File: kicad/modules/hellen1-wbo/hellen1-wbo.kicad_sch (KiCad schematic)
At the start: 59 parts, among them J600 Conn_02x03_Odd_Even, M600 Module-wbo-0.3, Q600 BTS3028, Q601 VNP28N04-E, U600 MCP6004, U601 AD8628, U602 STM32F042K6Tx, U603 REF3033, U604 XC6206P332MR

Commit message: add can
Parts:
- added C617, C618: 100n, Capacitor_SMD:C_0402_1005Metric, symbol hellen1-wbo-rescue:C-Device
- added D603: PESD1CAN, Package_TO_SOT_SMD:SOT-23, symbol semiconductors:PESD1CAN
- added R629: 120, Resistor_SMD:R_0402_1005Metric, symbol hellen1-wbo-rescue:R-Device
- added U605: TJA1051T/3/1J, Package_SO:SO-8_3.9x4.9mm_P1.27mm, symbol Transceivers:TJA1051T/3/1J
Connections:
- net +5V: now also C617.1, U605.3 (VCC)
- net CAN_RX: now also U605.4 (RXD)
- net CAN_TX: now also U605.1 (TXD)
- net GND: now also C617.2, C618.2, D603.3 (S), U605.2 (GND), U605.8 (S)
- new net CANH: D603.2 (D), R629.1, U605.6 (CANL)
- new net CANL: D603.1 (G), R629.2, U605.7 (CANH)
- new net CANVIO: C618.1, U605.5 (VIO)
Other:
- moved on the sheet: C605, R607, R610, R611, R612, U600C

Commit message: adding CAN
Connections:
- net CANVIO is gone; now on net +3V3: C618.1, U605.5 (VIO)
- net CANH: now also M600.W3 (CANH)
- net CANL: now also M600.W4 (CANL)
- net CAN_RX: no longer M600.W3 (CAN_RX)
- net CAN_TX: no longer M600.W4 (CAN_TX)
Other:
- moved on the sheet: C617, C618, D603, R629, U605

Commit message: new wbo module
правки

финал
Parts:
- M600: value Module-wbo-0.3 -> Module-wbo-0.4; footprint hellen-one-wbo-0.3:wbo -> hellen-one-wbo-0.4:wbo; symbol hellen-one-wbo-0.3:Module-wbo-0.3 -> hellen-one-wbo-0.4:Module-wbo-0.4
- renumbered D603 to D604
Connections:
- net GND: now also U602.2 (PF0), U602.3 (PF1)
- no-connect marks 11 -> 9
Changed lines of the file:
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@@
   (junction (at 68.58 114.3) (diameter 0) (color 0 0 0 0)
   )
+  (junction (at 175.895 85.09) (diameter 0) (color 0 0 0 0)
+  )
   (junction (at 186.055 61.595) (diameter 1.016) (color 0 0 0 0)
   )
@@
   (no_connect (at 175.895 97.79))
   (no_connect (at 201.295 107.95))
-  (no_connect (at 175.895 82.55))
   (no_connect (at 201.295 92.71))
   (no_connect (at 201.295 95.25))
@@
   (no_connect (at 261.62 35.56))
   (no_connect (at 201.295 82.55))
-  (no_connect (at 175.895 85.09))
   (no_connect (at 201.295 80.01))
   (wire (pts (xy 64.77 123.19) (xy 64.77 111.76))
@@
     (stroke (width 0) (type solid) (color 0 0 0 0))
   )
+  (wire (pts (xy 171.45 85.09) (xy 175.895 85.09))
+    (stroke (width 0) (type solid) (color 0 0 0 0))
+  )
   (wire (pts (xy 120.65 87.63) (xy 118.11 87.63))
     (stroke (width 0) (type solid) (color 0 0 0 0))
@@
     (stroke (width 0) (type solid) (color 0 0 0 0))
   )
+  (wire (pts (xy 175.895 85.09) (xy 175.895 82.55))
+    (stroke (width 0) (type default) (color 0 0 0 0))
+  )
   (wire (pts (xy 27.94 32.385) (xy 27.94 34.925))
     (stroke (width 0) (type solid) (color 0 0 0 0))
@@
     (pin "1")
   )
+  (symbol (lib_id "hellen1-wbo-rescue:GND-power") (at 171.45 85.09 0) (mirror y) (unit 1)
+    (in_bom yes) (on_board yes)
+    (property "Reference" "#PWR?" (id 0) (at 171.45 91.44 0)
+      (effects (font (size 1.27 1.27)) hide)
+    )
+    (property "Value" "GND" (id 1) (at 171.323 89.4842 0))
+    (property "Footprint" "" (id 2) (at 171.45 85.09 0)
+      (effects (font (size 1.27 1.27)) hide)
+    )
+    (property "Datasheet" "" (id 3) (at 171.45 85.09 0)
+      (effects (font (size 1.27 1.27)) hide)
+    )
+    (pin "1")
+  )
   (symbol (lib_id "hellen1-wbo-rescue:GND-power") (at 36.83 111.76 270) (mirror x) (unit 1)
     (in_bom yes) (on_board yes)
-    (property "Reference" "#PWR?" (id 0) (at 30.48 111.76 0)
+    (property "Reference" "#PWR0105" (id 0) (at 30.48 111.76 0)
       (effects (font (size 1.27 1.27)) hide)
     )
@@
   (symbol (lib_id "hellen1-wbo-rescue:GND-power") (at 53.34 109.22 90) (mirror x) (unit 1)
     (in_bom yes) (on_board yes)
-    (property "Reference" "#PWR?" (id 0) (at 59.69 109.22 0)
+    (property "Reference" "#PWR0103" (id 0) (at 59.69 109.22 0)
       (effects (font (size 1.27 1.27)) hide)
     )
@@
   (symbol (lib_id "hellen1-wbo-rescue:GND-power") (at 50.8 95.25 90) (mirror x) (unit 1)
     (in_bom yes) (on_board yes)
-    (property "Reference" "#PWR?" (id 0) (at 57.15 95.25 0)
+    (property "Reference" "#PWR0101" (id 0) (at 57.15 95.25 0)
       (effects (font (size 1.27 1.27)) hide)
     )
@@
   (symbol (lib_id "hellen1-wbo-rescue:GND-power") (at 53.34 124.46 0) (unit 1)
     (in_bom yes) (on_board yes)
-    (property "Reference" "#PWR?" (id 0) (at 53.34 130.81 0)
+    (property "Reference" "#PWR0102" (id 0) (at 53.34 130.81 0)
       (effects (font (size 1.27 1.27)) hide)
     )
@@
   (symbol (lib_id "hellen1-wbo-rescue:+5V-power") (at 33.02 114.3 90) (mirror x) (unit 1)
     (in_bom yes) (on_board yes)
-    (property "Reference" "#PWR?" (id 0) (at 36.83 114.3 0)
+    (property "Reference" "#PWR0106" (id 0) (at 36.83 114.3 0)
       (effects (font (size 1.27 1.27)) hide)
     )
@@
     (pin "1")
   )
-  (symbol (lib_id "hellen-one-wbo-0.3:Module-wbo-0.3") (at 168.91 121.92 0) (unit 1)
+  (symbol (lib_id "hellen-one-wbo-0.4:Module-wbo-0.4") (at 168.91 121.92 0) (unit 1)
     (in_bom yes) (on_board yes) (fields_autoplaced)
     (property "Reference" "M600" (id 0) (at 185.42 118.0804 0))
-    (property "Value" "Module-wbo-0.3" (id 1) (at 185.42 120.8555 0))
-    (property "Footprint" "hellen-one-wbo-0.3:wbo" (id 2) (at 194.31 120.65 0)
+    (property "Value" "Module-wbo-0.4" (id 1) (at 185.42 120.8555 0))
+    (property "Footprint" "hellen-one-wbo-0.4:wbo" (id 2) (at 194.31 120.65 0)
       (effects (font (size 1.27 1.27)) hide)
     )
@@
   (symbol (lib_id "semiconductors:PESD1CAN") (at 44.45 93.98 0) (unit 1)
     (in_bom yes) (on_board yes) (fields_autoplaced)
-    (property "Reference" "D603" (id 0) (at 45.085 87.63 0))
+    (property "Reference" "D604" (id 0) (at 45.085 87.63 0))
     (property "Value" "PESD1CAN" (id 1) (at 45.085 90.17 0))
     (property "Footprint" "Package_TO_SOT_SMD:SOT-23" (id 2) (at 46.99 101.6 0)
@@
   (symbol (lib_id "hellen1-wbo-rescue:+3.3V-power") (at 59.69 116.84 270) (unit 1)
     (in_bom yes) (on_board yes)
-    (property "Reference" "#PWR?" (id 0) (at 55.88 116.84 0)
+    (property "Reference" "#PWR0104" (id 0) (at 55.88 116.84 0)
       (effects (font (size 1.27 1.27)) hide)
     )
@@
   (symbol (lib_id "hellen1-wbo-rescue:GND-power") (at 33.02 127 0) (unit 1)
     (in_bom yes) (on_board yes)
-    (property "Reference" "#PWR?" (id 0) (at 33.02 133.35 0)
+    (property "Reference" "#PWR0107" (id 0) (at 33.02 133.35 0)
       (effects (font (size 1.27 1.27)) hide)
     )
@@
       (reference "#PWR06") (unit 1) (value "GND") (footprint "")
     )
+    (path "/44785bce-4456-4ddc-8cf6-356164e72c3d"
+      (reference "#PWR0101") (unit 1) (value "GND") (footprint "")
+    )
+    (path "/7f18c641-d6ab-4e4b-a1c1-b87a496a921f"
+      (reference "#PWR0102") (unit 1) (value "GND") (footprint "")
+    )
+    (path "/1599f7c6-42c9-4ed4-9f84-643ab6fb748b"
+      (reference "#PWR0103") (unit 1) (value "GND") (footprint "")
+    )
+    (path "/ed8e311e-c975-4faf-a433-017b3873da94"
+      (reference "#PWR0104") (unit 1) (value "+3.3V") (footprint "")
+    )
+    (path "/14787ae6-6b54-4bd7-b8f0-1795f2cb9d81"
+      (reference "#PWR0105") (unit 1) (value "GND") (footprint "")
+    )
+    (path "/aead63d5-a153-407c-9b85-6855dacc77a1"
+      (reference "#PWR0106") (unit 1) (value "+5V") (footprint "")
+    )
+    (path "/f8a1bf12-8885-4b79-8b83-39101450a636"
+      (reference "#PWR0107") (unit 1) (value "GND") (footprint "")
+    )
     (path "/00000000-0000-0000-0000-00005eb130b2"
       (reference "#PWR0600") (unit 1) (value "GND") (footprint "")
@@
       (reference "#PWR0649") (unit 1) (value "GND") (footprint "")
     )
-    (path "/14787ae6-6b54-4bd7-b8f0-1795f2cb9d81"
-      (reference "#PWR?") (unit 1) (value "GND") (footprint "")
-    )
-    (path "/1599f7c6-42c9-4ed4-9f84-643ab6fb748b"
-      (reference "#PWR?") (unit 1) (value "GND") (footprint "")
-    )
-    (path "/44785bce-4456-4ddc-8cf6-356164e72c3d"
-      (reference "#PWR?") (unit 1) (value "GND") (footprint "")
-    )
-    (path "/7f18c641-d6ab-4e4b-a1c1-b87a496a921f"
-      (reference "#PWR?") (unit 1) (value "GND") (footprint "")
-    )
-    (path "/aead63d5-a153-407c-9b85-6855dacc77a1"
-      (reference "#PWR?") (unit 1) (value "+5V") (footprint "")
-    )
-    (path "/ed8e311e-c975-4faf-a433-017b3873da94"
-      (reference "#PWR?") (unit 1) (value "+3.3V") (footprint "")
-    )
-    (path "/f8a1bf12-8885-4b79-8b83-39101450a636"
+    (path "/10ca8d1d-9815-4280-9786-a73150972327"
       (reference "#PWR?") (unit 1) (value "GND") (footprint "")
     )
@@
     )
     (path "/e36a7df6-df10-493f-b2bc-66bdf2551b00"
-      (reference "D603") (unit 1) (value "PESD1CAN") (footprint "Package_TO_SOT_SMD:SOT-23")
+      (reference "D604") (unit 1) (value "PESD1CAN") (footprint "Package_TO_SOT_SMD:SOT-23")
     )
     (path "/c2a04a62-ac6a-4516-8378-213e846aba4a"
@@
     )
     (path "/b31bd6a2-d597-4ef3-ad7d-f0d5e79bcc1c"
-      (reference "M600") (unit 1) (value "Module-wbo-0.3") (footprint "hellen-one-wbo-0.3:wbo")
+      (reference "M600") (unit 1) (value "Module-wbo-0.4") (footprint "hellen-one-wbo-0.4:wbo")
     )
     (path "/00000000-0000-0000-0000-0000600e1a2d"

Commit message: add blue text
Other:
- note added: "GPIO pins PF0, PF1 connected to ground to improve the routing (floating pins by the software)."
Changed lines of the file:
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@@
+    (effects (font (size 1.27 1.27)) (justify left bottom))
+  )
+  (text "GPIO pins PF0, PF1 connected \nto ground to improve the routing\n(floating pins by the software)."
+    (at 135.89 82.55 0)
     (effects (font (size 1.27 1.27)) (justify left bottom))
   )

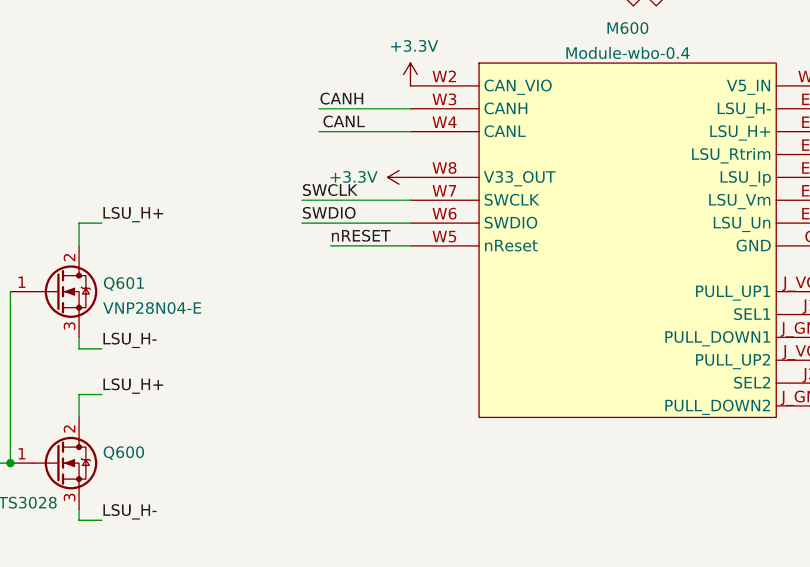
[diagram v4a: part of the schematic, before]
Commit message: added 9th input pin - VDDA
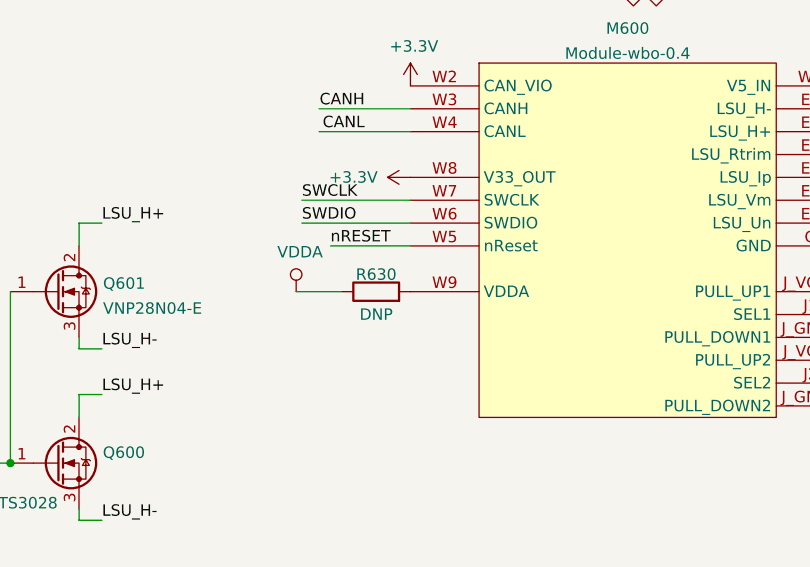
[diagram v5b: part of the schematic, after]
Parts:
- added R630: DNP, Resistor_SMD:R_0402_1005Metric, symbol hellen1-wbo-rescue:R-Device
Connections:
- net VDDA: now also R630.1
- new net: M600.W9 (VDDA), R630.2
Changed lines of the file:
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@@
     (stroke (width 0) (type default) (color 0 0 0 0))
   )
+  (wire (pts (xy 148.59 147.32) (xy 153.67 147.32))
+    (stroke (width 0) (type default) (color 0 0 0 0))
+  )
   (wire (pts (xy 33.02 114.3) (xy 36.83 114.3))
     (stroke (width 0) (type default) (color 0 0 0 0))
@@
   (symbol (lib_id "hellen1-wbo-rescue:GND-power") (at 171.45 85.09 0) (mirror y) (unit 1)
     (in_bom yes) (on_board yes)
-    (property "Reference" "#PWR?" (id 0) (at 171.45 91.44 0)
+    (property "Reference" "#PWR0108" (id 0) (at 171.45 91.44 0)
       (effects (font (size 1.27 1.27)) hide)
     )
@@
     (pin "1")
   )
+  (symbol (lib_id "hellen1-wbo-rescue:VDDA-power") (at 148.59 147.32 0) (unit 1)
+    (in_bom yes) (on_board yes)
+    (property "Reference" "#PWR0109" (id 0) (at 148.59 151.13 0)
+      (effects (font (size 1.27 1.27)) hide)
+    )
+    (property "Value" "VDDA" (id 1) (at 149.0218 142.9258 0))
+    (property "Footprint" "" (id 2) (at 148.59 147.32 0)
+      (effects (font (size 1.27 1.27)) hide)
+    )
+    (property "Datasheet" "" (id 3) (at 148.59 147.32 0)
+      (effects (font (size 1.27 1.27)) hide)
+    )
+    (pin "1")
+  )
   (symbol (lib_id "Transistor_FET:VNP10N07") (at 121.92 147.32 0) (unit 1)
     (in_bom yes) (on_board yes) (fields_autoplaced)
@@
     (pin "1")
   )
+  (symbol (lib_id "hellen1-wbo-rescue:R-Device") (at 157.48 147.32 90) (unit 1)
+    (in_bom yes) (on_board yes)
+    (property "Reference" "R630" (id 0) (at 157.48 145.415 90))
+    (property "Value" "DNP" (id 1) (at 157.48 149.86 90))
+    (property "Footprint" "Resistor_SMD:R_0402_1005Metric" (id 2) (at 157.48 149.098 90)
+      (effects (font (size 1.27 1.27)) hide)
+    )
+    (property "Datasheet" "~" (id 3) (at 157.48 147.32 0)
+      (effects (font (size 1.27 1.27)) hide)
+    )
+    (property "LCSC" "C17168" (id 4) (at 157.48 147.32 0)
+      (effects (font (size 1.27 1.27)) hide)
+    )
+    (pin "1")
+    (pin "2")
+  )
   (symbol (lib_id "hellen1-wbo-rescue:GND-power") (at 209.55 142.24 90) (unit 1)
     (in_bom yes) (on_board yes)
@@
     (pin "W7")
     (pin "W8")
+    (pin "W9")
   )
   (symbol (lib_id "hellen1-wbo-rescue:GND-power") (at 209.55 160.02 90) (unit 1)
@@
       (reference "#PWR0107") (unit 1) (value "GND") (footprint "")
     )
+    (path "/10ca8d1d-9815-4280-9786-a73150972327"
+      (reference "#PWR0108") (unit 1) (value "GND") (footprint "")
+    )
+    (path "/48baa104-d05e-4eed-a021-5654a78a6884"
+      (reference "#PWR0109") (unit 1) (value "VDDA") (footprint "")
+    )
     (path "/00000000-0000-0000-0000-00005eb130b2"
       (reference "#PWR0600") (unit 1) (value "GND") (footprint "")
@@
       (reference "#PWR0649") (unit 1) (value "GND") (footprint "")
     )
-    (path "/10ca8d1d-9815-4280-9786-a73150972327"
-      (reference "#PWR?") (unit 1) (value "GND") (footprint "")
-    )
     (path "/00000000-0000-0000-0000-00005eb1294f"
       (reference "C600") (unit 1) (value "1u") (footprint "Capacitor_SMD:C_0402_1005Metric")
@@
       (reference "R629") (unit 1) (value "120") (footprint "Resistor_SMD:R_0402_1005Metric")
     )
+    (path "/8719995c-7a59-4520-a953-b0d876dea9a1"
+      (reference "R630") (unit 1) (value "DNP") (footprint "Resistor_SMD:R_0402_1005Metric")
+    )
     (path "/00000000-0000-0000-0000-00005f8980df"

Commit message: removed LCSC number for DNP
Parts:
- R630: LCSC C17168 -> (none)
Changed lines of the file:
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@@
       (effects (font (size 1.27 1.27)) hide)
     )
-    (property "LCSC" "C17168" (id 4) (at 157.48 147.32 0)
+    (property "LCSC" "" (id 4) (at 157.48 147.32 0)
       (effects (font (size 1.27 1.27)) hide)
     )

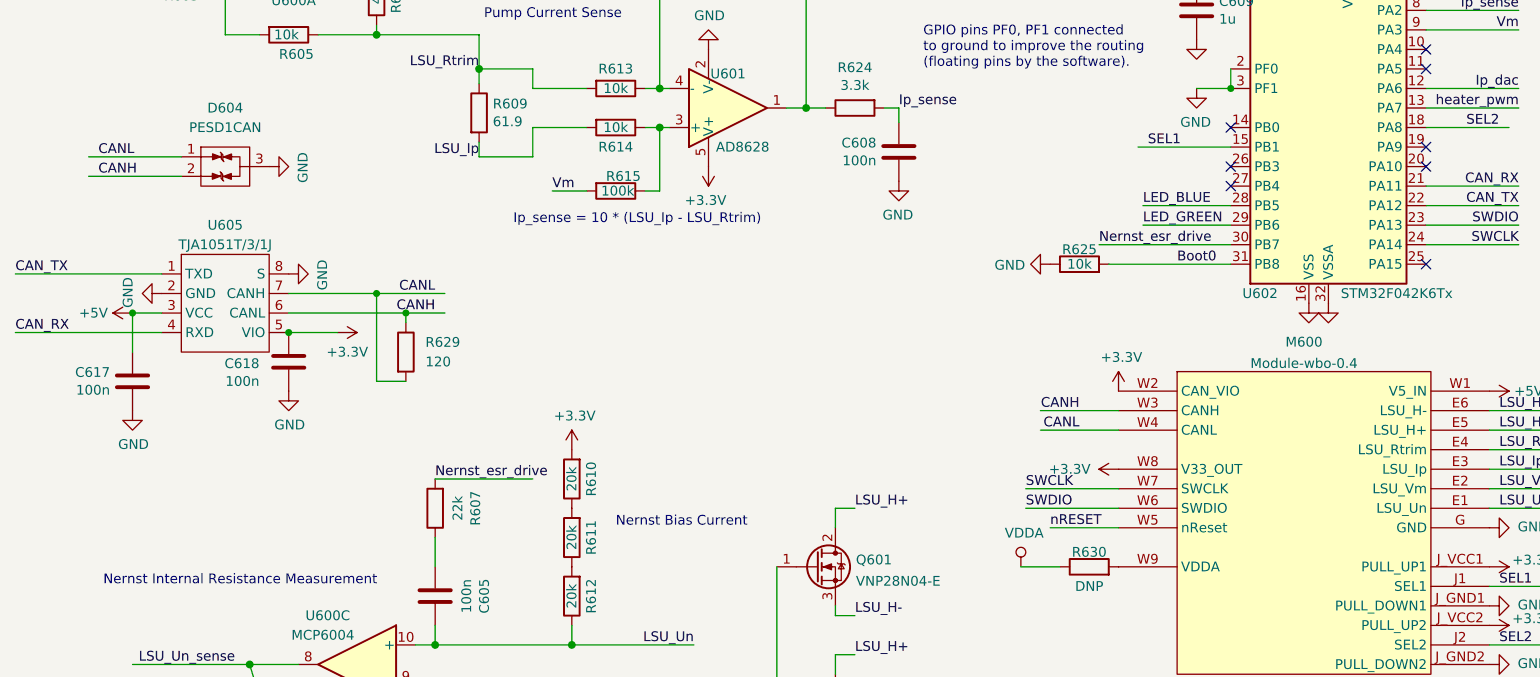
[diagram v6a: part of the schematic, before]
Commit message: #281 CANH and CANL aren`t flipped now
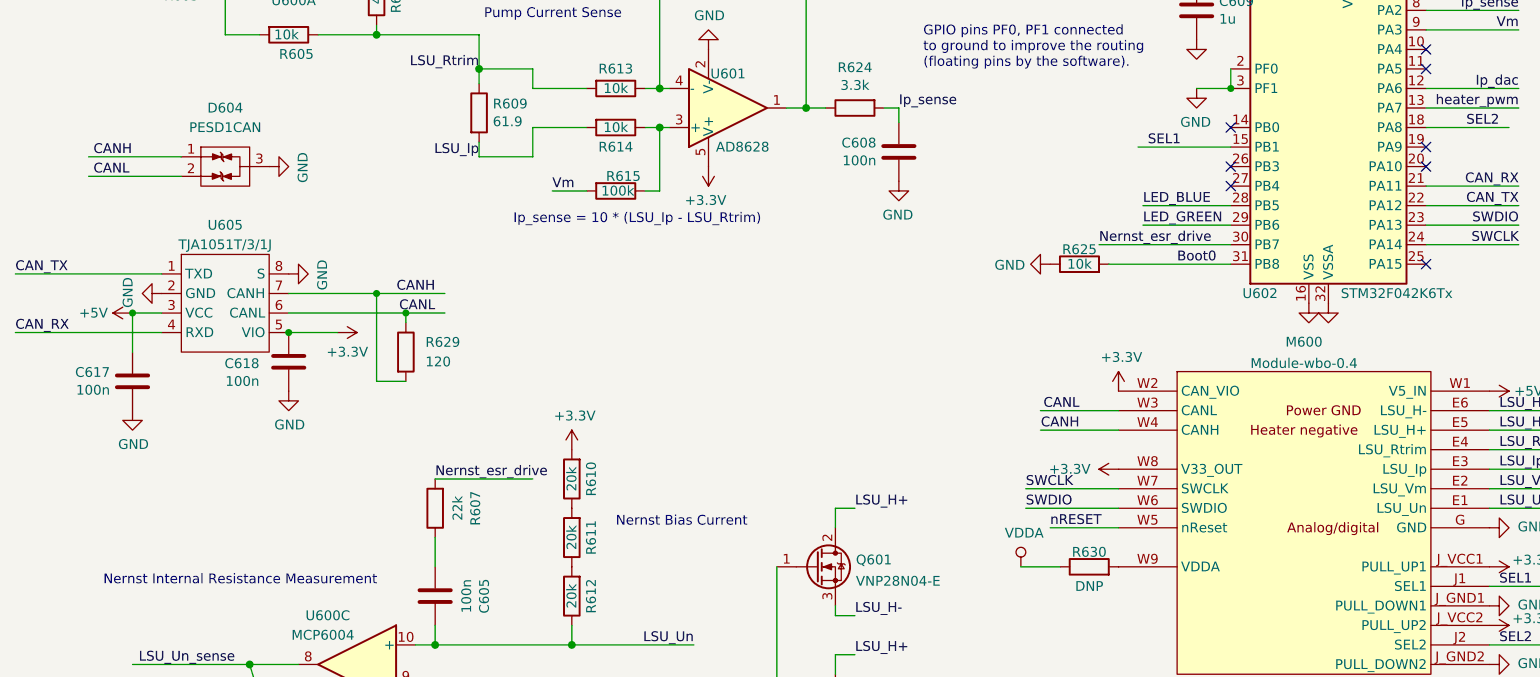
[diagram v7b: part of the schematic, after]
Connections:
- net CANH: now also D604.1 (G), M600.W4 (CANH), R629.2, U605.7 (CANH); no longer D604.2 (D), M600.W3 (CANH), R629.1, U605.6 (CANL)
- net CANL: now also D604.2 (D), M600.W3 (CANL), R629.1, U605.6 (CANL); no longer D604.1 (G), M600.W4 (CANL), R629.2, U605.7 (CANH)
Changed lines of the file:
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@@
     (effects (font (size 1.27 1.27)) (justify left bottom))
   )
-  (label "CANH" (at 72.39 114.3 180)
+  (label "CANH" (at 72.39 111.76 180)
     (effects (font (size 1.27 1.27)) (justify right bottom))
   )
@@
     (effects (font (size 1.27 1.27)) (justify right bottom))
   )
-  (label "CANH" (at 28.575 96.52 0)
+  (label "CANH" (at 27.94 93.98 0)
     (effects (font (size 1.27 1.27)) (justify left bottom))
   )
@@
     (effects (font (size 1.27 1.27)) (justify left bottom))
   )
-  (label "CANL" (at 28.575 93.98 0)
+  (label "CANL" (at 27.94 96.52 0)
     (effects (font (size 1.27 1.27)) (justify left bottom))
   )
@@
     (effects (font (size 1.27 1.27)) (justify right bottom))
   )
-  (label "CANH" (at 156.21 127 180)
+  (label "CANH" (at 156.21 129.54 180)
     (effects (font (size 1.27 1.27)) (justify right bottom))
   )
-  (label "CANL" (at 72.39 111.76 180)
+  (label "CANL" (at 72.39 114.3 180)
     (effects (font (size 1.27 1.27)) (justify right bottom))
   )
@@
     (effects (font (size 1.27 1.27)) (justify left bottom))
   )
-  (label "CANL" (at 156.21 129.54 180)
+  (label "CANL" (at 156.21 127 180)
     (effects (font (size 1.27 1.27)) (justify right bottom))
   )
